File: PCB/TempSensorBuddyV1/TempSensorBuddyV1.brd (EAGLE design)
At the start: 160 x 100 mm, 8 parts, among them U1 MAX30205

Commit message: Review changes complete. Starting layout
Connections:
- net +3V3: no longer U1.5, U1.6, U1.7
- net GND: now also U1.5, U1.6, U1.7
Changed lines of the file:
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@@
 <contactref element="R2" pad="2"/>
 <contactref element="C1" pad="1"/>
+<contactref element="PWR" pad="A"/>
+<contactref element="R3" pad="2"/>
 <contactref element="U1" pad="8"/>
-<contactref element="R3" pad="2"/>
-<contactref element="U1" pad="5"/>
-<contactref element="U1" pad="6"/>
-<contactref element="U1" pad="7"/>
-<contactref element="PWR" pad="A"/>
-<wire x1="-26.92" y1="4.8" x2="-27.42" y2="4.8" width="0" layer="19" extent="1-1"/>
-<wire x1="-26.42" y1="4.8" x2="-26.92" y2="4.8" width="0" layer="19" extent="1-1"/>
-<wire x1="-25.92" y1="4.8" x2="-26.42" y2="4.8" width="0" layer="19" extent="1-1"/>
-<wire x1="-20.78" y1="2.54" x2="-25.92" y2="4.8" width="0" layer="19" extent="1-1"/>
-<wire x1="-23.71" y1="11.43" x2="-25.92" y2="4.8" width="0" layer="19" extent="1-1"/>
+<wire x1="-20.78" y1="2.54" x2="-27.42" y2="4.8" width="0" layer="19" extent="1-1"/>
+<wire x1="-23.71" y1="11.43" x2="-27.42" y2="4.8" width="0" layer="19" extent="1-1"/>
 <wire x1="-22.01" y1="17.78" x2="-23.71" y2="11.43" width="0" layer="19" extent="1-1"/>
 <wire x1="-27.09" y1="17.78" x2="-22.01" y2="17.78" width="0" layer="19" extent="1-1"/>
@@
 <contactref element="U1" pad="9"/>
 <contactref element="R4" pad="1"/>
+<contactref element="U1" pad="5"/>
+<contactref element="U1" pad="6"/>
+<contactref element="U1" pad="7"/>
 <wire x1="-26.67" y1="3.81" x2="-25.92" y2="2.82" width="0" layer="19" extent="1-1"/>
-<wire x1="-22.01" y1="11.43" x2="-26.67" y2="3.81" width="0" layer="19" extent="1-1"/>
+<wire x1="-26.42" y1="4.8" x2="-26.67" y2="3.81" width="0" layer="19" extent="1-1"/>
+<wire x1="-25.92" y1="4.8" x2="-26.42" y2="4.8" width="0" layer="19" extent="1-1"/>
+<wire x1="-26.92" y1="4.8" x2="-26.42" y2="4.8" width="0" layer="19" extent="1-1"/>
+<wire x1="-22.01" y1="11.43" x2="-25.92" y2="4.8" width="0" layer="19" extent="1-1"/>
 <wire x1="-18.63" y1="17.78" x2="-22.01" y2="11.43" width="0" layer="19" extent="1-1"/>
 <wire x1="-14.78" y1="2.54" x2="-25.92" y2="2.82" width="0" layer="19" extent="1-1"/>

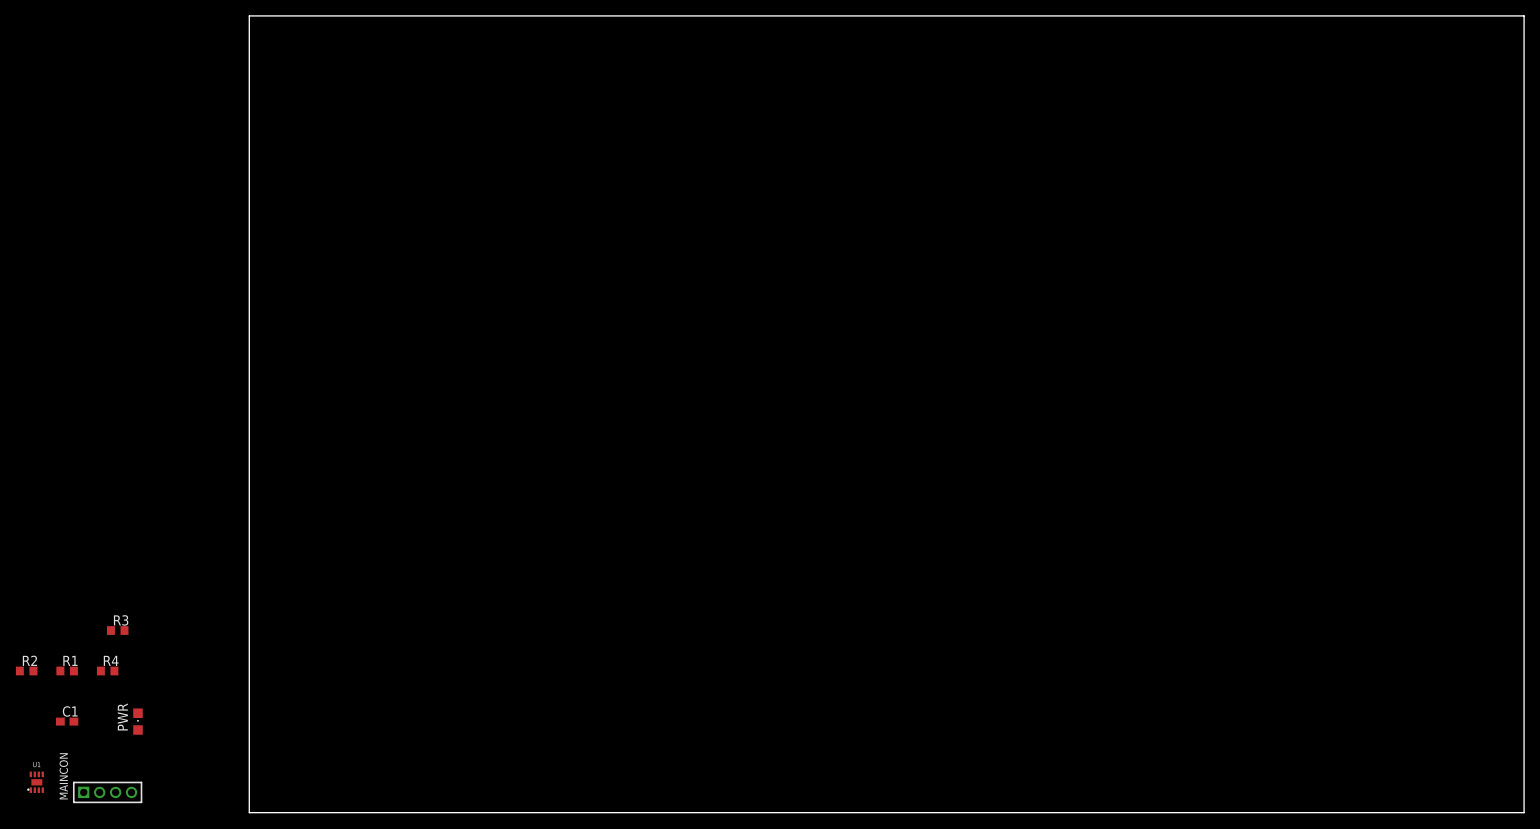
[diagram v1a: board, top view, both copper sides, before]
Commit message: Finished routing Temp Buddy Board. Please review.
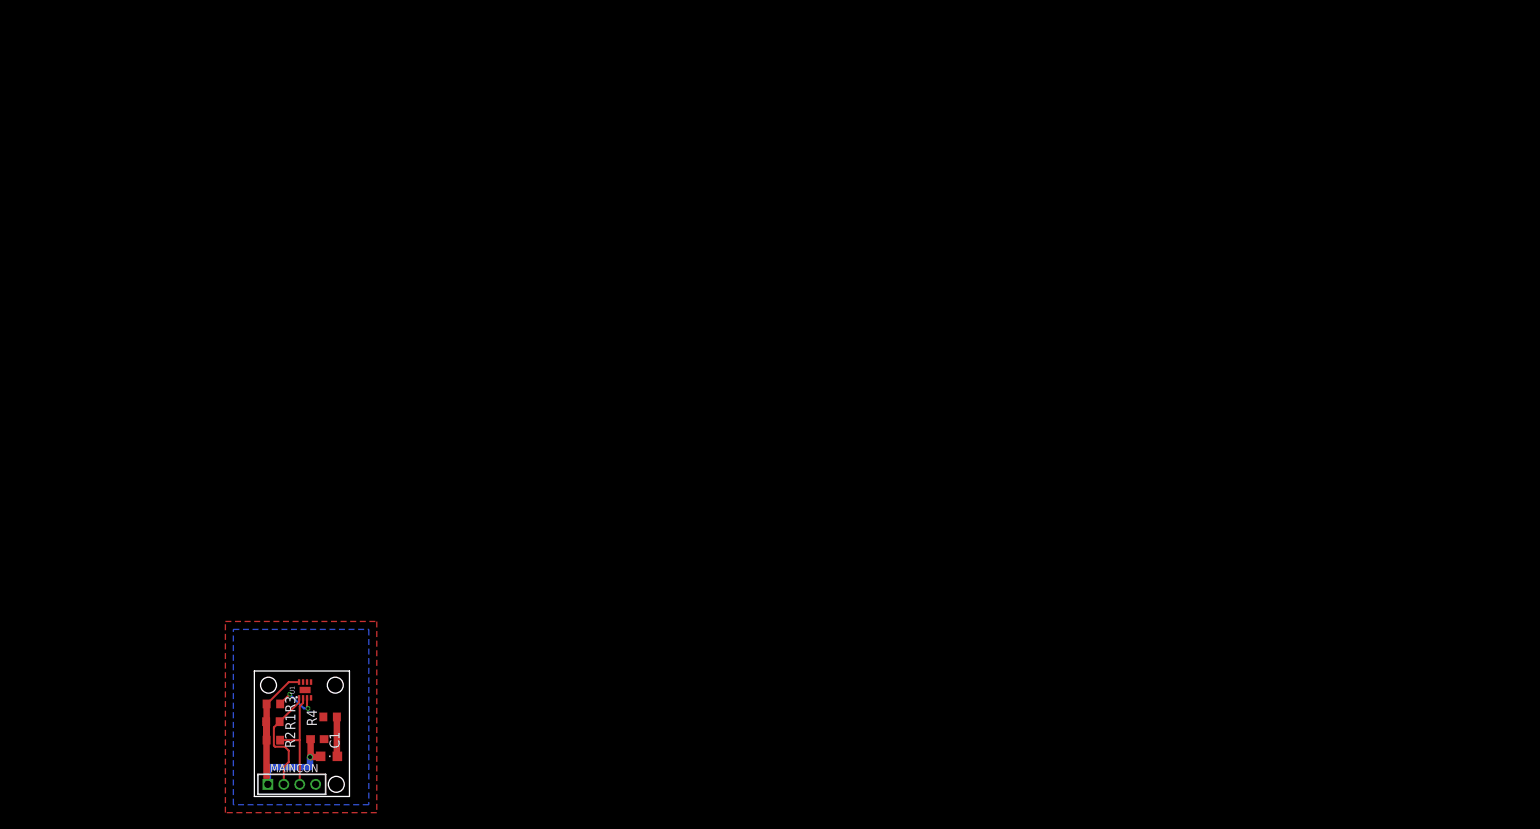
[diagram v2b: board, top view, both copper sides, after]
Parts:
- moved U1 35.6 mm to (7.00, 15.4)
- moved R2 32.1 mm to (3.02, 9.10), turned to 180 degrees
- moved C1 31.5 mm to (8.54, 9.23)
- moved R4 28.5 mm to (10.1, 12.0)
- moved R1 26.6 mm to (2.96, 11.4), turned to 180 degrees
- moved PWR 24.4 mm to (10.0, 7.07), turned to 270 degrees
- moved MAINCON 23.1 mm to (5.33, 3.56)
- moved R3 21.6 mm to (3.02, 13.7), turned to 180 degrees
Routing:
- net +3V3: track 0.00 -> 30.1 mm, vias 0 -> 1
- net SDA: track 0.00 -> 13.9 mm
- net SCL: track 0.00 -> 13.5 mm
- net N$1: track 0.00 -> 6.11 mm, vias 0 -> 2
- net N$3: track 0.00 -> 4.97 mm
- added copper zone on layer 1, net GND
- added copper zone on layer 16, net GND
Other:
- board size 160 x 100 mm -> 11.9 x 15.7 mm
